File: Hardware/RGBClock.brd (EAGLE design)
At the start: 81.3 x 81.3 mm, 89 parts, among them IC1 PTH08080W, IC2 LP2985-Digital, IC3 LP2985-Analog, IC4 MCP1824S, IC5 PTH08080W, Q1 MS5V, T1 IRF7205, T2 PUMH*, T3 SI2323, X1 NEB21R, X2 MICRO-SD3

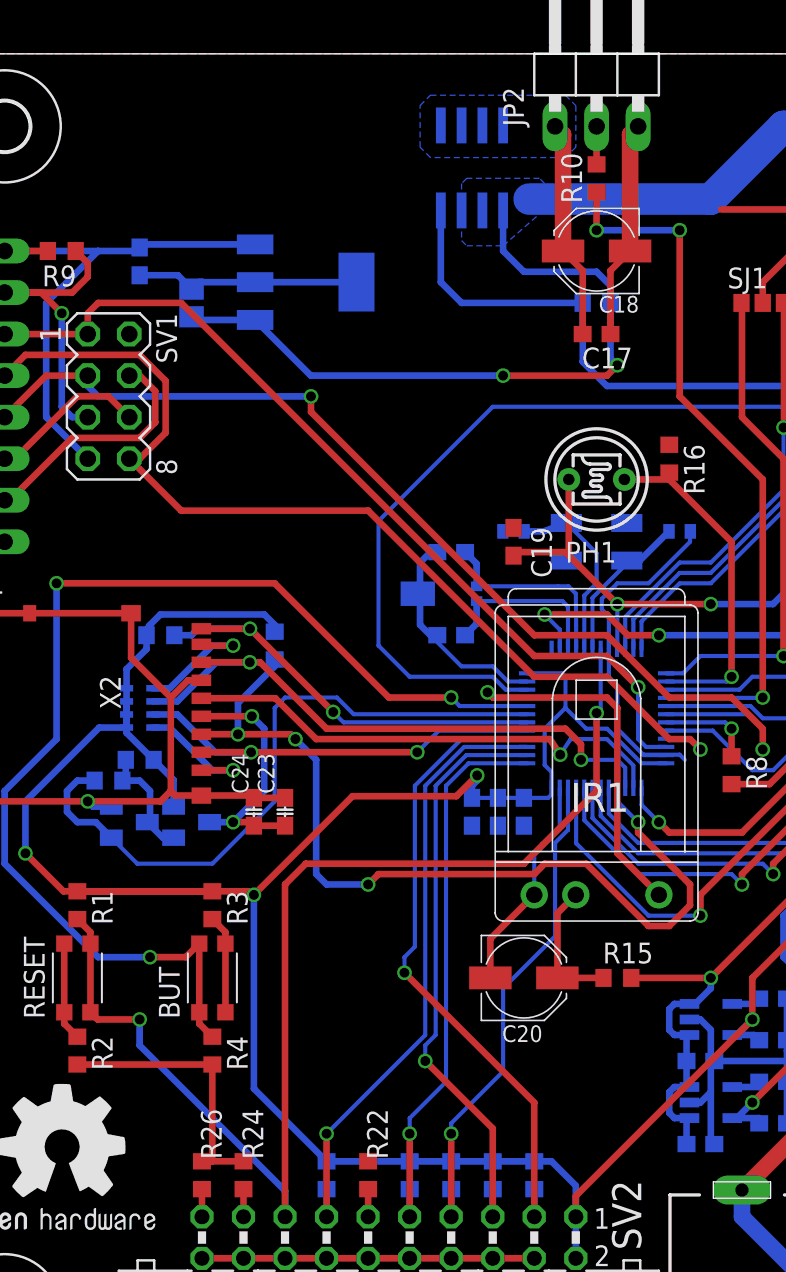
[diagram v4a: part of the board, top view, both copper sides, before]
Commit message: minor changes on silkscreen
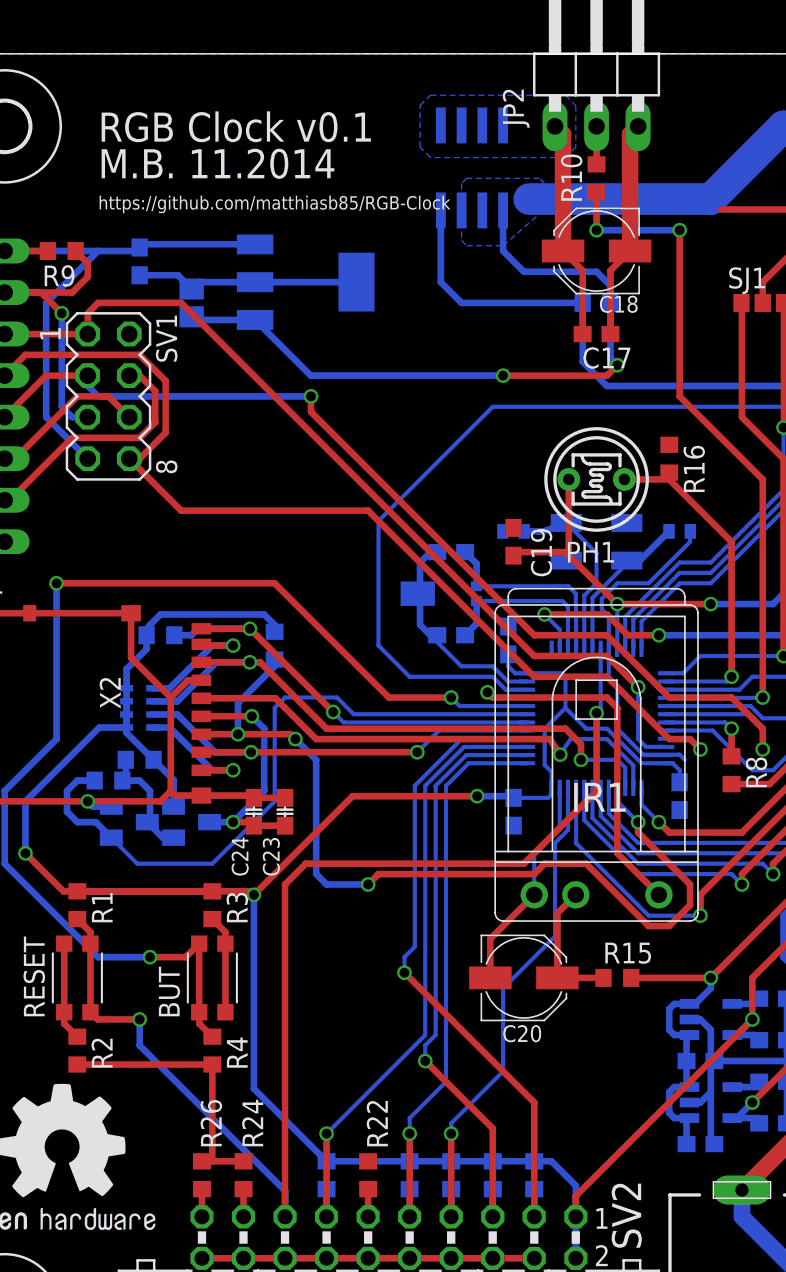
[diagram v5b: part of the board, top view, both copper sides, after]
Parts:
- moved C21 10.5 mm to (35.2, 45.4), turned to 90 degrees
- moved C25 9.57 mm to (45.7, 35.9)
- moved C22 2.54 mm to (35.6, 34.9)
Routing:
- net +3V3: track 192.5 -> 194.0 mm
